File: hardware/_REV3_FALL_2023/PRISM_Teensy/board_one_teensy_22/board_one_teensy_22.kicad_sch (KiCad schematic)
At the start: 20 parts, among them J2 PRISM_IO_INTERFACE, J3 3387, U1 Teensy4.0, U2 GPS-14414, U3 3966, U4 RFM69HCW_Breakout, U5 SFN-1407PA7.6

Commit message: Procrastinated PRISM commit
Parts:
- removed D3, D4: 1655, LED_1655, symbol neopixel:1655
- removed J2: PRISM_IO_INTERFACE, symbol Connector_Generic:Conn_01x11
- removed U2: GPS-14414, GPS_layout:GPS-14414, symbol GPS:GPS-14414
- added C3: 0.1uf, Capacitor_SMD:C_0603_1608Metric, symbol Device:C
- added D3: WS2812B, LED_SMD:LED_WS2812B_PLCC4_5.0x5.0mm_P3.2mm, symbol LED:WS2812B
- added J1: Micro_SD_Card_Det_Hirose_DM3AT, OEM:DM3CS-SF_HIR, symbol Connector:Micro_SD_Card_Det_Hirose_DM3AT
- added J4: Conn_01x14, symbol Connector_Generic:Conn_01x14
- added R1, R2, R3: 10k, Resistor_SMD:R_0603_1608Metric, symbol Device:R
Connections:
- net 3.3V: now also C3.2, J1.4 (VDD), J4.12 (Pin_12), R1.2, R3.1
- net 5V: now also D5.1 (VDD), D3.1 (VDD), J4.2 (Pin_2)
- net ARM: now also J4.6 (Pin_6)
- net CONT 1: now also J4.7 (Pin_7)
- net CONT 2: now also J4.8 (Pin_8)
- net DIR: now also J4.11 (Pin_11)
- net EN: now also J4.9 (Pin_9)
- net GND: now also D5.3 (VSS), C3.1, D3.3 (VSS), J1.6 (VSS), J4.1 (Pin_1)
- net PYRO 1: now also J4.4 (Pin_4)
- net PYRO 2: now also J4.5 (Pin_5)
- net SCL 1: now also J4.13 (Pin_13)
- net SDA 1: now also J4.14 (Pin_14)
- net STEP: now also J4.10 (Pin_10)
- net V_SENSE: now also J4.3 (Pin_3)
- net at D5.2 (DOUT): now also D3.4 (DIN)
- net SD_Detect: now reaches U1.11 (9_OUT1C)
- net SD_Detect: now also J1.9 (DET_B)
- net SD_CS: now reaches U1.12 (10_CS_MQSR)
- net SD_CS: now also J1.3 (CMD)
- net SD_MOSI: now reaches U1.13 (11_MOSI_CTX1)
- net SD_MOSI: now also J1.7 (DAT0)
- net SD_MISO: now reaches U1.14 (12_MISO_MQSL)
- net SD_MISO: now also J1.2 (DAT3/CD)
- net SD_SCK: now reaches U1.20 (13_SCK_CRX1_LED)
- net SD_SCK: now also J1.5 (CLK)
- new net: J1.10 (DET_A), R1.1, R2.2
- new net: J1.8 (DAT1), R2.1
- new net: J1.1 (DAT2), R3.2
- no-connect marks 32 -> 27
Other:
- note removed: "GPS"
- moved on the sheet: C2, D5

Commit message: Finalized PRISM schematic
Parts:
- removed D1, D2: SS54, JLC_footprints:DO-214AC, symbol SS54:SS54
- J3: footprint 3387 -> MPL3115A2_barometer:MPL3115A2
- J4: footprint (none) -> Connector_JST:JST_XH_B14B-XH-A_1x14_P2.50mm_Vertical
- R4: value 200K -> 56k
- R5: value 300K -> 15k
- U3: footprint BMP388:Adafruit_Industries-3966-MFG -> Personal:MPL3115A2
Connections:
- net SCL 1 is gone; now on net TX_GPS: J4.13 (Pin_13)
- net SDA 1 is gone; now on net RX_GPS: J4.14 (Pin_14)
- net SD_MISO is gone; now on net MISO: J1.2 (DAT3/CD), U1.14 (12_MISO_MQSL)
- net SD_MOSI is gone; now on net MOSI: J1.7 (DAT0), U1.13 (11_MOSI_CTX1)
- net TX 5 is gone; now on net Radio_RST: U4.9 (RST)
- net CS 1: now also U1.8 (6_OUT1D)
- net RX_GPS: now reaches U1.2 (0_RX1_CRX2_CS1)
- net TX_GPS: now reaches U1.3 (1_TX1_CTX2_MISO1)
- net V_Mon: now reaches U1.30 (23_A9_CRX1_MCLK1)
- net V_Mon: now also R4.2, R5.1
- net Radio_RST: now reaches U1.7 (5_IN2)
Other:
- moved on the sheet: R4, R5

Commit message: Fix some issues with PRISM FC schematic
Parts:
- removed J4: Conn_01x14, Connector_JST:JST_XH_B14B-XH-A_1x14_P2.50mm_Vertical, symbol Connector_Generic:Conn_01x14
- added GPS/Stepper: Conn_01x02_Socket, Connector_JST:JST_XH_B2B-XH-A_1x02_P2.50mm_Vertical, symbol Connector:Conn_01x05_Socket
- added J2: Conn_01x04_Socket, symbol Connector:Conn_01x04_Socket
- added Power: Conn_01x04_Socket, Connector_JST:JST_XH_B4B-XH-A_1x04_P2.50mm_Vertical, symbol Connector:Conn_01x04_Socket
- added Pyro: Conn_01x05_Socket, Connector_JST:JST_XH_B5B-XH-A_1x05_P2.50mm_Vertical, symbol Connector:Conn_01x05_Socket
- J1: footprint OEM:DM3CS-SF_HIR -> DM3CS-SF:HRS_DM3CS-SF
- U1: footprint Teensy_4.1:Teensy40 -> DEV-15583:MODULE_DEV-15583; symbol Teensy_4.1:Teensy4.0 -> DEV-15583:DEV-15583; Availability (none) -> In Stock; Check_prices (none) -> https://www.snapeda.com/parts/DEV-15583/SparkFun+Electronic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; MANUFACTURER (none) -> Sparkfun; MAXIMUM_PACKAGE_HEIGHT (none) -> 5.87mm; MF (none) -> SparkFun Electronics; MP (none) -> DEV-15583; Package (none) -> None; Price (none) -> None; Purchase-URL (none) -> https://www.snapeda.com/api/url_track_click_mouser/?unipart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; STANDARD (none) -> Manufacturer Recommendations; SnapEDA_Link (none) -> https://www.snapeda.com/parts/DEV-15583/SparkFun+Electronic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
- U3: footprint Personal:MPL3115A2 -> BMP388:Adafruit_Industries-3966-MFG
- U4: footprint Sensors:RFM69HCW_Breakout -> RFM:RFM69HCW_Breakout
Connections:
- net RX_GPS is gone; now on net PYRO 2: U1.2
- net SCK is gone; now on net SD_SCK: U4.5 (SCK)
- net TX_GPS is gone; now on net CONT 1: U1.3
- net 3.3V: now also U1.3.3V_1, U1.3.3V_2, J2.1 (Pin_1), Power.1 (Pin_1); no longer U1.31 (3V3)
- net 5V: now also U1.VIN, J2.2 (Pin_2), Power.2 (Pin_2); no longer U1.33 (VIN)
- net ARM: now also U1.0, Pyro.1 (Pin_1); no longer U1.37 (26_A12_MOSI1)
- net BUZZER: now also U1.6; no longer U1.18 (PROGRAM)
- net CONT 1: now also Pyro.2 (Pin_2); no longer U1.27 (20_A6_TX5_LRCLK1)
- net CONT 2: now also U1.4, Pyro.3 (Pin_3); no longer U1.28 (21_A7_RX5_BCLK1)
- net CS 1: now also U1.9; no longer U1.8 (6_OUT1D)
- net DIR: now also U1.20, GPS/Stepper.4 (Pin_4)
- net EN: now also U1.5, GPS/Stepper.3 (Pin_3)
- net GND: now also U1.G1, U1.G2, U1.G3, J2.4 (Pin_4), Power.4 (Pin_4); no longer U1.1 (GND), U1.32 (GND)
- net MISO: now also U1.12; no longer U1.14 (12_MISO_MQSL)
- net MOSI: now also U1.11; no longer U1.13 (11_MOSI_CTX1)
- net NEOPIXEL: now also D5.4 (DIN), U1.22; no longer U1.45 (34_DAT1_MISO2)
- net PYRO 1: now also U1.1, Pyro.4 (Pin_4); no longer U1.35 (24_A10_TX6_SCL2)
- net PYRO 2: now also Pyro.5 (Pin_5); no longer U1.36 (25_A11_RX6_SDA2)
- net RX 5: now also U1.7
- net Radio_RST: now also U1.8; no longer U1.7 (5_IN2)
- net SCL 0: now also U1.19; no longer U1.26 (19_A5_SCL0)
- net SDA 0: now also U1.18; no longer U1.25 (18_A4_SDA0)
- net SD_CS: now also U1.10; no longer U1.12 (10_CS_MQSR)
- net SD_Detect: now also U1.14; no longer U1.11 (9_OUT1C)
- net SD_SCK: now also U1.13; no longer U1.20 (13_SCK_CRX1_LED)
- net STEP: now also U1.15, GPS/Stepper.5 (Pin_5)
- net V_Mon: now also U1.23; no longer U1.30 (23_A9_CRX1_MCLK1)
- net SCL 1: now reaches U1.16
- net SCL 1: now also GPS/Stepper.2 (Pin_2)
- net SDA 1: now reaches U1.17
- net SDA 1: now also GPS/Stepper.1 (Pin_1)
- net VIN renamed VBAT
- net VBAT: now also J2.3 (Pin_3), Power.3 (Pin_3)
- removed net V_SENSE: U1.38 (27_A13_SCK1)
- no-connect marks 27 -> 30
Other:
- moved on the sheet: C1, C2, R4, R5

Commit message: Finish PRISM FC schematic
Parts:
- removed H1: MountingHole_Pad, MountingHole:MountingHole_3.2mm_M3_DIN965_Pad_TopBottom, symbol Mechanical:MountingHole_Pad
- removed J2: Conn_01x04_Socket, symbol Connector:Conn_01x04_Socket
- added H1: MountingHole, MountingHole:MountingHole_3.2mm_M3_DIN965_Pad_TopBottom, symbol Mechanical:MountingHole
- D3, D5: footprint LED_SMD:LED_WS2812B_PLCC4_5.0x5.0mm_P3.2mm -> rocketry_footprints:WS2812B
- J1: footprint DM3CS-SF:HRS_DM3CS-SF -> rocketry_footprints:HRS_DM3CS-SF
- J3: footprint MPL3115A2_barometer:MPL3115A2 -> rocketry_footprints:3387
- U1: footprint DEV-15583:MODULE_DEV-15583 -> rocketry_footprints:MODULE_DEV-15583
- U3: footprint BMP388:Adafruit_Industries-3966-MFG -> rocketry_footprints:Adafruit_Industries-3966-MFG
- U4: footprint RFM:RFM69HCW_Breakout -> rocketry_footprints:RFM69HCW_Breakout
- U5: footprint buzzers:SFN-1407PA7.6 -> rocketry_footprints:SFN-1407PA7.6
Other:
- note added: "RADIO"
- note removed: "Radio"
- moved on the sheet: C3, J1, R1, R2, R3, R4, R5

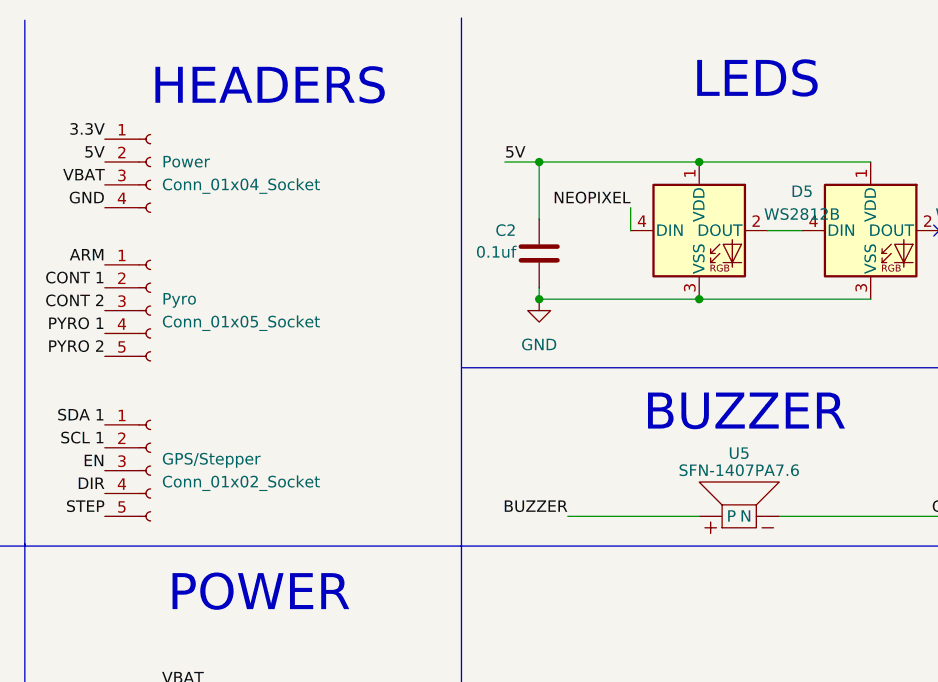
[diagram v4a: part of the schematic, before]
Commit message: Fix file name issue
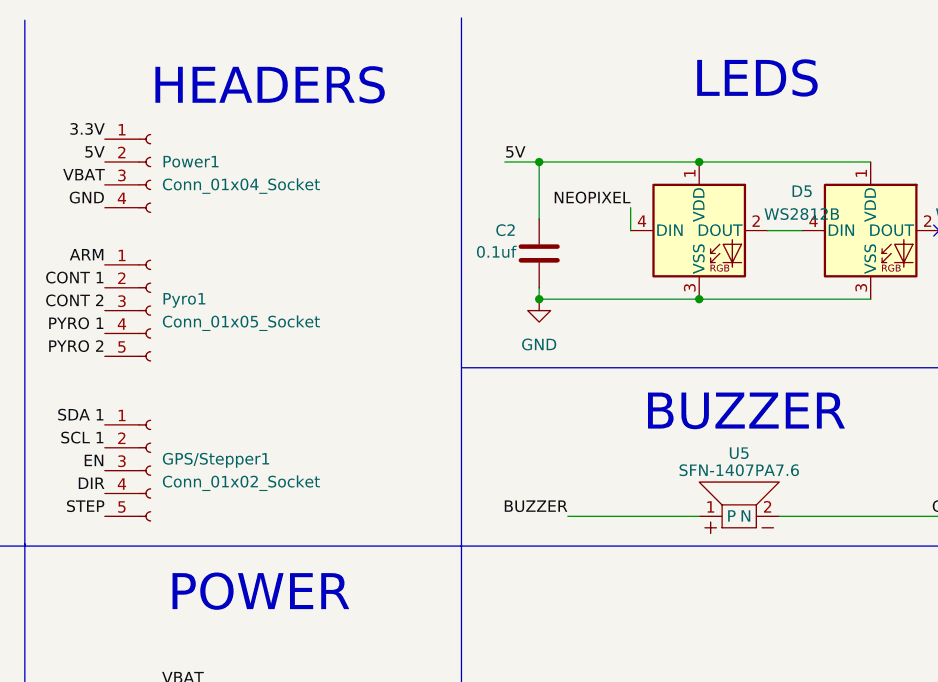
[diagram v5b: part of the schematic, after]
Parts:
- renumbered GPS/Stepper to GPS/Stepper1, Power to Power1, Pyro to Pyro1
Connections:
- net BUZZER: now also U5.1 (P); no longer U5. (P)
- net GND: now also U5.2 (N); no longer U5. (P)
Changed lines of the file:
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@@
   (symbol (lib_id "Connector:Conn_01x04_Socket") (at 187.96 27.94 0) (unit 1)
     (in_bom yes) (on_board yes) (dnp no) (fields_autoplaced)
-    (property "Reference" "Power" (at 189.23 27.94 0)
+    (property "Reference" "Power1" (at 189.23 27.94 0)
       (effects (font (size 1.27 1.27)) (justify left))
     )
@@
       (project "board_one_teensy_22"
         (path "/7a48c3b0-2761-409e-ae2f-7ebae3820225"
-          (reference "Power") (unit 1)
+          (reference "Power1") (unit 1)
         )
       )
@@
       (effects (font (size 1.27 1.27)) hide)
     )
-    (pin "")
-    (pin "")
+    (pin "2")
+    (pin "1")
     (instances
       (project "board_one_teensy_22"
@@
   (symbol (lib_id "Connector:Conn_01x05_Socket") (at 187.96 44.45 0) (unit 1)
     (in_bom yes) (on_board yes) (dnp no) (fields_autoplaced)
-    (property "Reference" "Pyro" (at 189.23 43.18 0)
+    (property "Reference" "Pyro1" (at 189.23 43.18 0)
       (effects (font (size 1.27 1.27)) (justify left))
     )
@@
       (project "board_one_teensy_22"
         (path "/7a48c3b0-2761-409e-ae2f-7ebae3820225"
-          (reference "Pyro") (unit 1)
+          (reference "Pyro1") (unit 1)
         )
       )
@@
   (symbol (lib_id "Connector:Conn_01x05_Socket") (at 187.96 62.23 0) (unit 1)
     (in_bom yes) (on_board yes) (dnp no) (fields_autoplaced)
-    (property "Reference" "GPS/Stepper" (at 189.23 60.96 0)
+    (property "Reference" "GPS/Stepper1" (at 189.23 60.96 0)
       (effects (font (size 1.27 1.27)) (justify left))
     )
@@
       (project "board_one_teensy_22"
         (path "/7a48c3b0-2761-409e-ae2f-7ebae3820225"
-          (reference "GPS/Stepper") (unit 1)
-        )
-      )
+          (reference "GPS/Stepper1") (unit 1)
+        )
+      )

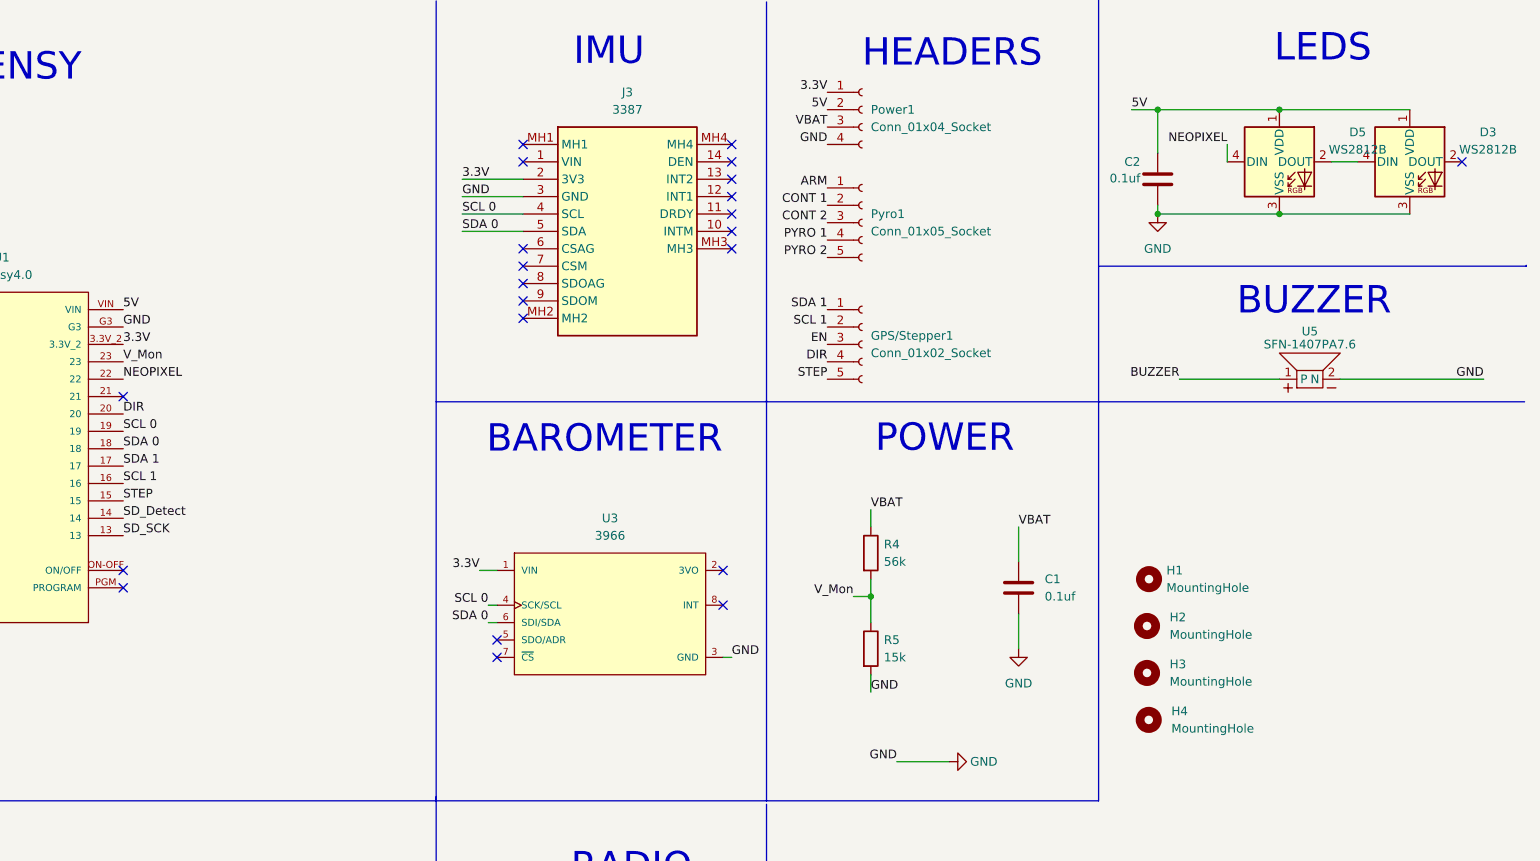
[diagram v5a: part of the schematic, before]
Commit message: Need to fix SD slot still
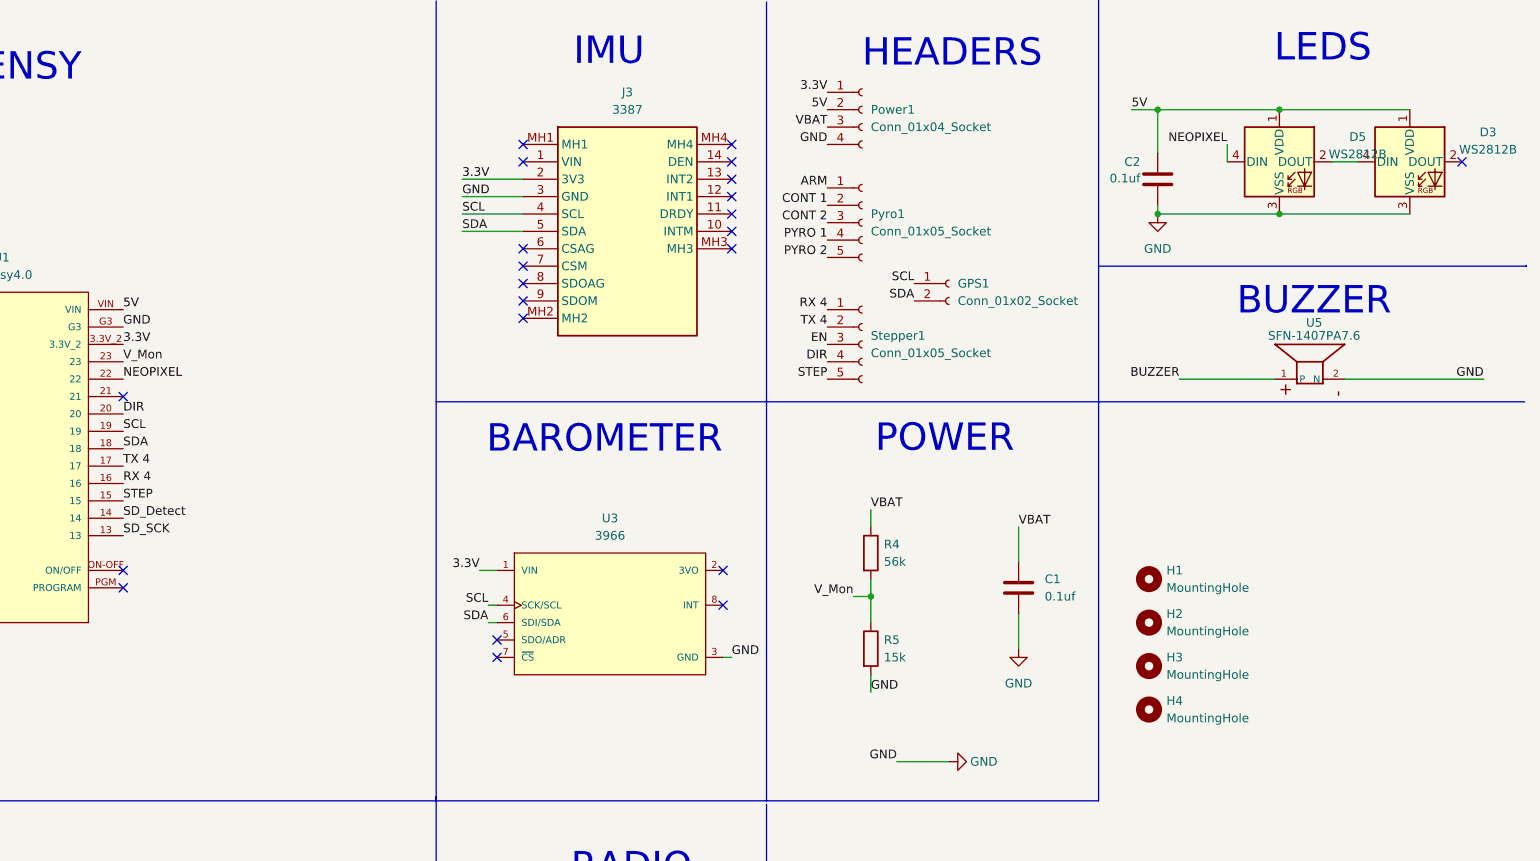
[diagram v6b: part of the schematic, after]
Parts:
- added GPS1: Conn_01x02_Socket, Connector_JST:JST_XH_B2B-XH-A_1x02_P2.50mm_Vertical, symbol Connector:Conn_01x02_Socket
- J3: footprint rocketry_footprints:3387 -> 3387; symbol LSM9DS1:3387 -> 3387:3387
- Stepper1: renamed from GPS/Stepper1; value Conn_01x02_Socket -> Conn_01x05_Socket; footprint Connector_JST:JST_XH_B2B-XH-A_1x02_P2.50mm_Vertical -> Connector_JST:JST_XH_B5B-XH-A_1x05_P2.50mm_Vertical
- U5: symbol SFN-1407PA7.6:SFN-1407PA7.6 -> SMT-0827-S-HT-R:SMT-0827-S-HT-R; MANUFACTURER (none) -> PUI Audio; MAXIMUM_PACKAGE_HEIGHT (none) -> 3.3mm; PARTREV (none) -> 31/03/20; STANDARD (none) -> Manufacturer Recommendations
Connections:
- net SCL 0 renamed SCL
- net SCL: now also GPS1.1 (Pin_1)
- net SCL 1 renamed RX 4
- net RX 4: now also Stepper1.1 (Pin_1); no longer Stepper1.2 (Pin_2)
- net SDA 0 renamed SDA
- net SDA: now also GPS1.2 (Pin_2)
- net SDA 1 renamed TX 4
- net TX 4: now also Stepper1.2 (Pin_2); no longer Stepper1.1 (Pin_1)

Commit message: PRISM FC built without errors
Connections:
- net 3.3V: now also R2.2; no longer R1.2
- net GND: now also R1.2, U1.14
- net SD_Detect: no longer names the net of J1.9 (DET_A)
- net SD_Detect: now also R1.1; no longer U1.14
- no-connect marks 30 -> 29
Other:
- moved on the sheet: C3, R1
